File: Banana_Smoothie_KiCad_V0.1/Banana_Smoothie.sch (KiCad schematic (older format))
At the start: 120 parts, among them IC1 LPC1769, IC5 LD117ADT33TR, Q1 BSL207SP, Q2 12MHz, SW1 SW_TACT_4P_B, SW3 SW_TACT_4P_B, U3 USD-SOCKETUSD, X14 USB

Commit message: Added LAN8720_Module
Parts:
- removed C26, C27: 220u, RCL_E2_5-7, symbol RCL_CPOL-EU
- removed D2: 214AC, DP_DEVICES_DO-214AC, symbol DP_DEVICES_DIODE
- removed IC2: ~, SmoothieBrainz - next round:LINEAR_TO263-5, symbol LINEAR_LM2596S
- removed L2: 33uH, SPARKFUN-PASSIVES_CDRH125, symbol SPARKFUN-PASSIVES_INDUCTOR
- added M1: LM2596_Module, Banana_Smoothie_Footprints:LM2596_Module, symbol LM2596_Module
- JP1: footprint PINHEAD_2X07_90 -> Banana_Smoothie_Footprints:LAN8720_Module
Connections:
- net labels removed: N$9
- wire segments 451 -> 437
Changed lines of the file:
@@
 EESchema Schematic File Version 2
-LIBS:Banana_SmoothieBrainz
+LIBS:Banana_Smoothie
 LIBS:power
 LIBS:Oscillators
@@
 $EndComp
 $Comp
-L RCL_CPOL-EU C26
-U 1 1 58522BC5
-P 19050 18150
-F 0 "C26" H 19095 18168 70  0000 L BNN
-F 1 "220u" H 19094 17969 70  0000 L BNN
-F 2 "RCL_E2_5-7" H 19040 17940 65  0001 L TNN
-F 3 "" H 19050 18150 60  0001 C CNN
-	1    19050 18150
-	1    0    0    -1
-$EndComp
-$Comp
-L RCL_CPOL-EU C27
-U 1 1 58522C8D
-P 20650 18150
-F 0 "C27" H 20695 18168 70  0000 L BNN
-F 1 "220u" H 20694 17969 70  0000 L BNN
-F 2 "RCL_E2_5-7" H 20640 17940 65  0001 L TNN
-F 3 "" H 20650 18150 60  0001 C CNN
-	1    20650 18150
-	1    0    0    -1
-$EndComp
-$Comp
 L RCL_C-EU C44
 U 1 1 58522E1D
@@
 $EndComp
 $Comp
-L DP_DEVICES_DIODE D2
-U 1 1 58523205
-P 20050 18250
-F 0 "D2" H 20150 18269 70  0000 L BNN
-F 1 "214AC" H 20040 18140 65  0001 L TNN
-F 2 "DP_DEVICES_DO-214AC" H 20040 18040 65  0001 L TNN
-F 3 "" H 20050 18250 60  0001 C CNN
-	1    20050 18250
-	0    -1   -1   0
-$EndComp
-$Comp
 L MICROBUILDER_DIODE D3
 U 1 1 585232CD
@@
 $EndComp
 $Comp
-L LINEAR_LM2596S IC2
-U 1 1 585241A5
-P 19550 18150
-F 0 "IC2" H 19250 18400 70  0000 L BNN
-F 1 "~" H 19540 18040 65  0001 L TNN
-F 2 "SmoothieBrainz - next round:LINEAR_TO263-5" H 19540 17940 65  0001 L TNN
-F 3 "" H 19550 18150 60  0001 C CNN
-	1    19550 18150
-	1    0    0    -1
-$EndComp
-$Comp
 L V-REG_LD117ADT33TR IC5
 U 1 1 5852426D
@@
 F 0 "JP1" H 12800 13574 70  0000 L BNN
 F 1 "JP1" H 13040 13040 65  0001 L TNN
-F 2 "PINHEAD_2X07_90" H 13040 12940 65  0001 L TNN
+F 2 "Banana_Smoothie_Footprints:LAN8720_Module" H 13040 12940 65  0001 L TNN
 F 3 "" H 13050 13150 60  0001 C CNN
 	1    13050 13150
@@
 $EndComp
 $Comp
-L SPARKFUN-PASSIVES_INDUCTOR L2
-U 1 1 5852507D
-P 20350 18050
-F 0 "L2" H 20450 18250 70  0000 L BNN
-F 1 "33uH" H 20450 17850 70  0000 L BNN
-F 2 "SPARKFUN-PASSIVES_CDRH125" H 20340 17840 65  0001 L TNN
-F 3 "" H 20350 18050 60  0001 C CNN
-	1    20350 18050
-	0    -1   -1   0
-$EndComp
-$Comp
 L LED_LED LED1
 U 1 1 58525145
@@
 Text Label 19050 16270 2    94   ~ 0
 5V
-Wire Wire Line
-	19950 18250 19950 18150
-Wire Wire Line
-	19950 18150 19750 18150
-Wire Wire Line
-	19750 18150 19750 17850
-Wire Wire Line
-	19750 17850 20650 17850
-Wire Wire Line
-	20650 17850 20650 18050
-Connection ~ 20650 18050
-Text Label 20650 17850 0    65   ~ 0
+Text Label 20600 18050 0    65   ~ 0
 5VREG
 Wire Wire Line
@@
 Text Label 11750 12950 0    65   ~ 0
 24V
-Wire Wire Line
-	19150 18050 19050 18050
-Wire Wire Line
-	19050 18050 19050 17950
-Connection ~ 19150 18050
-Connection ~ 19050 18050
-Text Label 18850 17950 0    65   ~ 0
+Text Label 18850 18000 0    65   ~ 0
 24V
 Wire Wire Line
@@
 GND
 Wire Wire Line
-	19150 18250 19150 18650
-Wire Wire Line
-	19150 18650 20650 18650
-Wire Wire Line
-	19550 18650 19550 18550
-Wire Wire Line
-	19650 18650 19650 18550
-Wire Wire Line
-	20050 18650 20050 18350
-Wire Wire Line
-	19150 18350 19050 18350
-Wire Wire Line
-	19050 18350 19050 18450
-Wire Wire Line
-	20050 18650 20750 18650
-Wire Wire Line
-	20650 18650 20650 18350
-Connection ~ 19550 18650
-Connection ~ 19650 18650
-Connection ~ 19150 18350
-Connection ~ 19150 18250
-Connection ~ 20050 18350
-Connection ~ 20050 18650
-Connection ~ 19050 18350
+	20900 18450 20550 18450
 Text Label 18850 18450 0    65   ~ 0
 GND
-Text Label 20750 18650 0    65   ~ 0
+Text Label 20700 18450 0    65   ~ 0
 GND
 Wire Wire Line
@@
 	16150 14950 16150 14750
 Wire Wire Line
-	19950 18050 20050 18050
-Wire Wire Line
-	20050 18050 20050 18150
-Connection ~ 20050 18050
-Connection ~ 19950 18050
-Wire Wire Line
 	16350 14950 16350 14750
 Wire Wire Line
@@
 Text GLabel 18750 16250 2    10   UnSpc ~ 0
 5V
-Text Label 20650 18050 0    10   ~ 0
-5VREG
-Text Label 19950 18250 0    10   ~ 0
-5VREG
-Text Label 20650 18050 1    10   ~ 0
+Text Label 20550 18050 0    10   ~ 0
 5VREG
 Text Label 18550 16250 2    10   ~ 0
@@
 Text Label 10950 12950 0    10   ~ 0
 24V
-Text Label 19150 18050 2    10   ~ 0
-24V
-Text Label 19050 18050 1    10   ~ 0
+Text Label 19050 18000 2    10   ~ 0
 24V
 Text Label 24950 23700 0    10   ~ 0
@@
 Text Label 10950 12550 0    10   ~ 0
 GND
-Text Label 19150 18250 2    10   ~ 0
-GND
-Text Label 19550 18550 3    10   ~ 0
-GND
-Text Label 19650 18550 3    10   ~ 0
+Text Label 19100 18450 0    10   ~ 0
 GND
-Text Label 20050 18350 3    10   ~ 0
-GND
-Text Label 19050 18350 3    10   ~ 0
-GND
-Text Label 20650 18350 3    10   ~ 0
+Text Label 20600 18450 0    10   ~ 0
 GND
 Text Label 10550 16950 1    10   ~ 0
@@
 Text Label 16150 14750 3    10   ~ 0
 N$8
-Text Label 19950 18050 0    10   ~ 0
-N$9
-Text Label 20050 18150 1    10   ~ 0
-N$9
-Text Label 20050 18050 2    10   ~ 0
-N$9
 Text Label 16350 14950 1    10   ~ 0
 N$10
@@
 	1    0    0    -1
 $EndComp
+$Comp
+L LM2596_Module M1
+U 1 1 5880D194
+P 19850 18250
+F 0 "M1" H 19550 18350 60  0000 C CNN
+F 1 "LM2596_Module" H 19850 18250 60  0000 C CNN
+F 2 "Banana_Smoothie_Footprints:LM2596_Module" H 19850 18250 60  0001 C CNN
+F 3 "" H 19850 18250 60  0001 C CNN
+	1    19850 18250
+	1    0    0    -1
+$EndComp
+Wire Wire Line
+	20550 18050 20850 18050
+Wire Wire Line
+	19200 18000 18850 18000
+Wire Wire Line
+	19200 18450 18850 18450
 $EndSCHEMATC

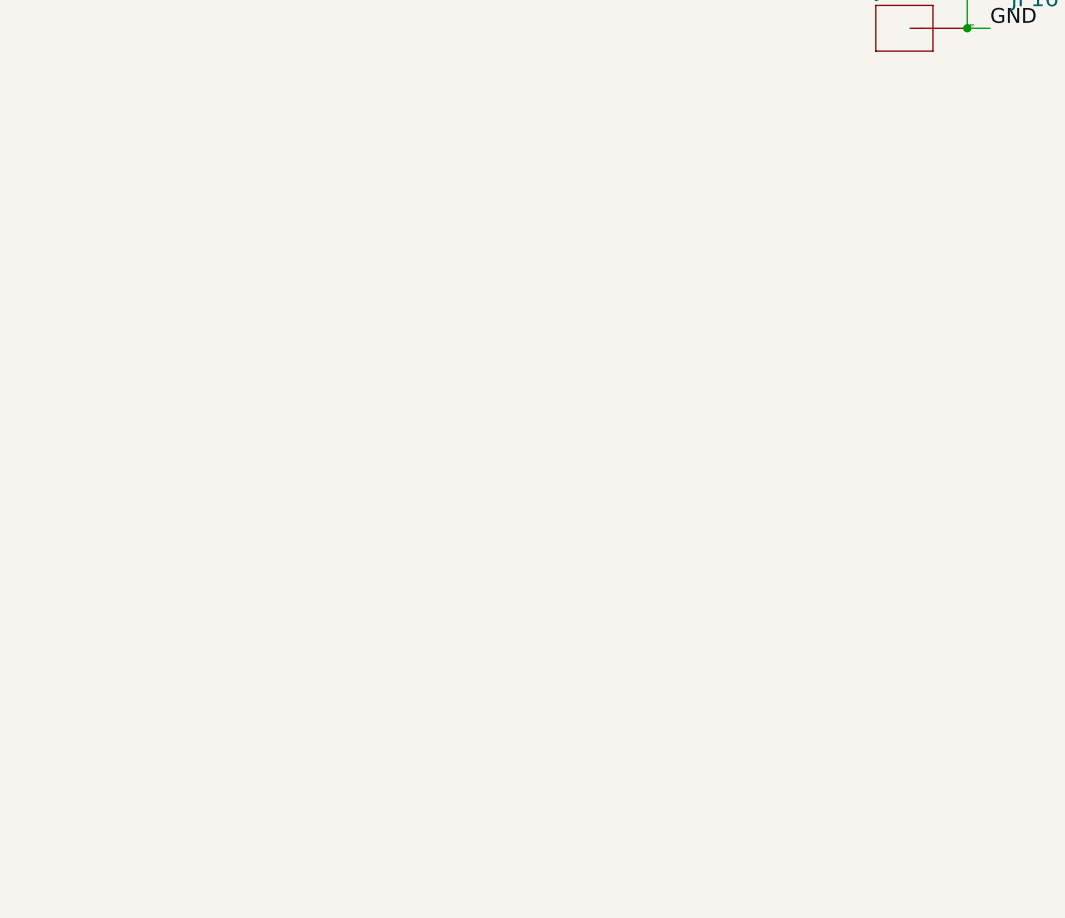
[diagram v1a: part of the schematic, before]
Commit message: Added reverse polarity protection
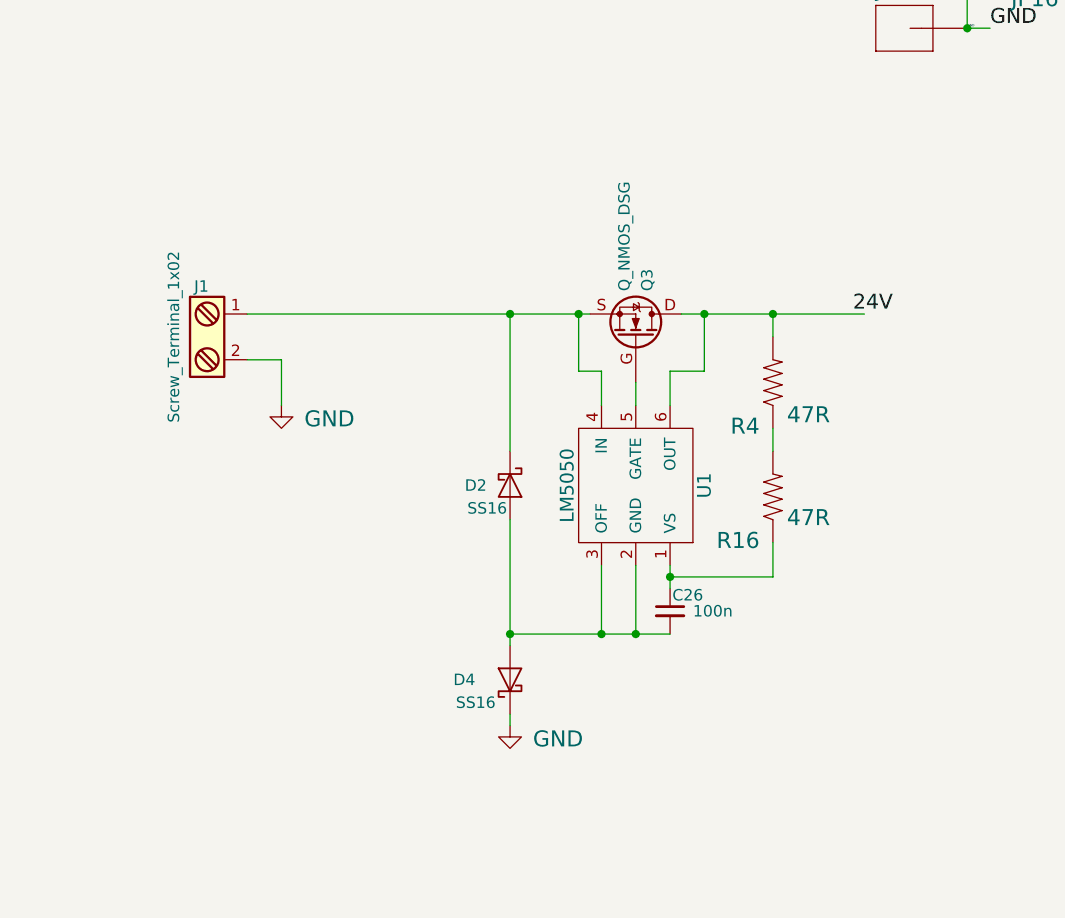
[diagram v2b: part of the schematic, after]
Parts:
- added C26: 100n, Capacitors_SMD:C_0603, symbol C_Small
- added D2, D4: SS16, Diodes_SMD:D_SMA_Standard, symbol D_Schottky
- added J1: Screw_Terminal_1x02, Connect:AK300-2, symbol Screw_Terminal_1x02
- added Q3: Q_NMOS_DSG, symbol Q_NMOS_DSG
- added R16, R4: 47R, Resistors_SMD:R_0402, symbol RESISTOR_R-US_
- added U1: LM5050, TO_SOT_Packages_SMD:SOT-23-6, symbol LM5050
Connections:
- wire segments 437 -> 459
